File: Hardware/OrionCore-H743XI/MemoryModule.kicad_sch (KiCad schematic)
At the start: 3 parts, among them U1 IS42S32800G-6BLI, U3 W25Q128JVP, U4 W25Q128JVP

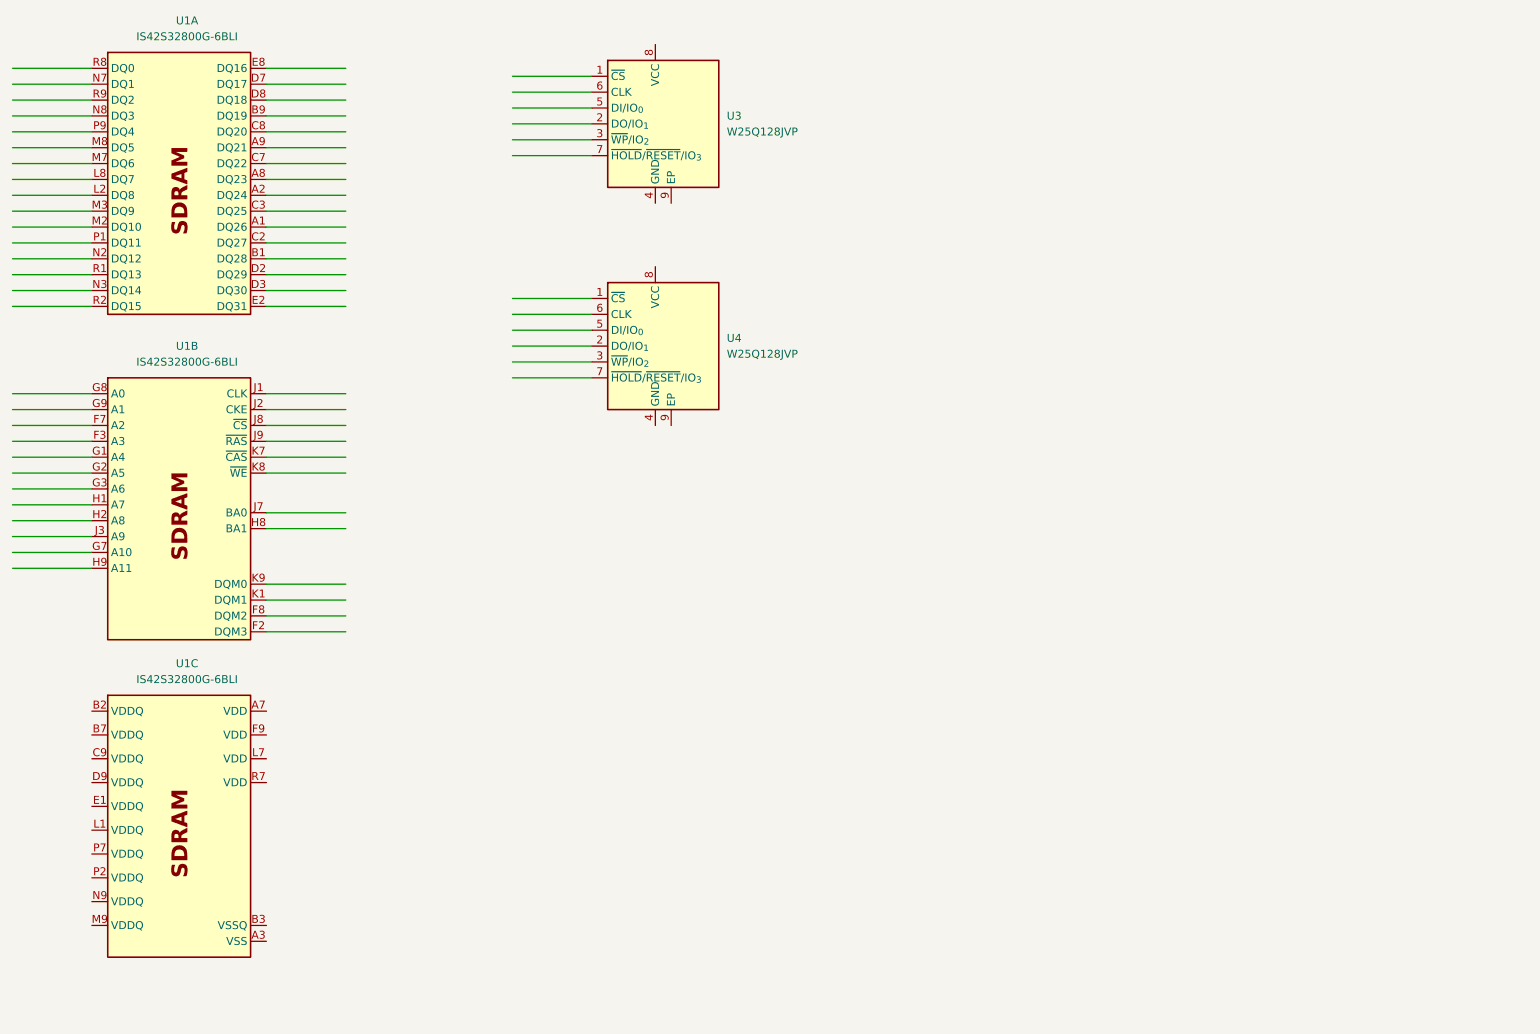
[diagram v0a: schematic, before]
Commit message: Update SDRAM, RGB LCD, QSPI Flash Pin
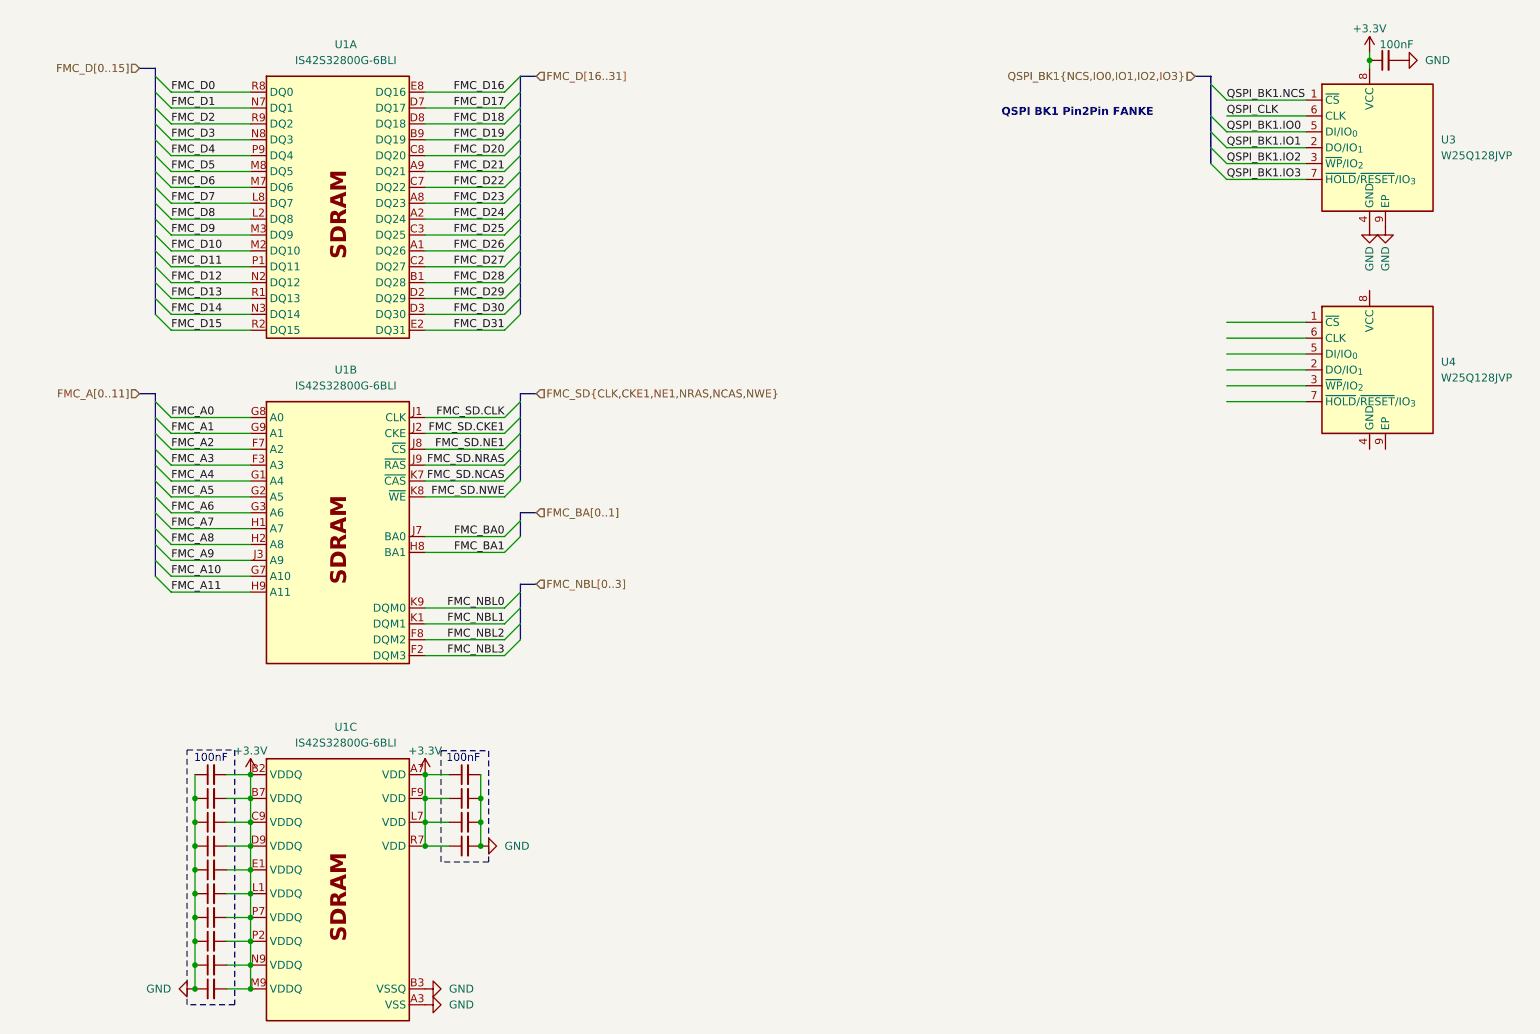
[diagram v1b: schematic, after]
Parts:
- added C30, C31, C32, C33, C34, C35, C36, C37, C38, C39, C40, C41, C42, C43, C44: 100nF, Capacitor_SMD:C_0201_0603Metric, symbol Device:C_Small
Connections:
- net VSS is gone; now on net GND: U1.A3 (VSS), U1.F1 (VSS), U1.L3 (VSS), U1.R3 (VSS)
- net VSSQ is gone; now on net GND: U1.B3 (VSSQ), U1.B8 (VSSQ), U1.C1 (VSSQ), U1.D1 (VSSQ), U1.E9 (VSSQ), U1.L9 (VSSQ), U1.M1 (VSSQ), U1.N1 (VSSQ), U1.P3 (VSSQ), U1.P8 (VSSQ)
- net QSPI_BK1.NCS: now reaches U3.1 (~{CS})
- net QSPI_BK1.IO1: now reaches U3.2 (DO/IO_{1})
- net QSPI_BK1.IO2: now reaches U3.3 (~{WP}/IO_{2})
- net GND: now reaches U3.4 (GND)
- net GND: now also U3.9 (EP), C30.1, C31.1, C32.1, C33.1, C34.1, C35.1, C36.1, C37.1, C38.1, C39.1, C40.2, C41.2, C42.2, C43.2, C44.2
- net QSPI_BK1.IO0: now reaches U3.5 (DI/IO_{0})
- net QSPI_CLK: now reaches U3.6 (CLK)
- net QSPI_BK1.IO3: now reaches U3.7 (~{HOLD}/~{RESET}/IO_{3})
- net +3.3V: now reaches U3.8 (VCC)
- net +3.3V: now also U1.A7 (VDD), U1.B2 (VDDQ), U1.B7 (VDDQ), U1.C9 (VDDQ), U1.D9 (VDDQ), U1.E1 (VDDQ), U1.F9 (VDD), U1.L1 (VDDQ), U1.L7 (VDD), U1.M9 (VDDQ), U1.N9 (VDDQ), U1.P2 (VDDQ), U1.P7 (VDDQ), U1.R7 (VDD), C30.2, C31.2, C32.2, C33.2, C34.2, C35.2, C36.2, C37.2, C38.2, C39.2, C40.1, C41.1, C42.1, C43.1, C44.1
- net FMC_D26: now reaches U1.A1 (DQ26)
- net FMC_D24: now reaches U1.A2 (DQ24)
- net FMC_D23: now reaches U1.A8 (DQ23)
- net FMC_D21: now reaches U1.A9 (DQ21)
- net FMC_D28: now reaches U1.B1 (DQ28)
- net FMC_D19: now reaches U1.B9 (DQ19)
- net FMC_D27: now reaches U1.C2 (DQ27)
- net FMC_D25: now reaches U1.C3 (DQ25)
- net FMC_D22: now reaches U1.C7 (DQ22)
- net FMC_D20: now reaches U1.C8 (DQ20)
- net FMC_D29: now reaches U1.D2 (DQ29)
- net FMC_D30: now reaches U1.D3 (DQ30)
- net FMC_D17: now reaches U1.D7 (DQ17)
- net FMC_D18: now reaches U1.D8 (DQ18)
- net FMC_D31: now reaches U1.E2 (DQ31)
- net FMC_D16: now reaches U1.E8 (DQ16)
- net FMC_D8: now reaches U1.L2 (DQ8)
- net FMC_D7: now reaches U1.L8 (DQ7)
- net FMC_D10: now reaches U1.M2 (DQ10)
- net FMC_D9: now reaches U1.M3 (DQ9)
- net FMC_D6: now reaches U1.M7 (DQ6)
- net FMC_D5: now reaches U1.M8 (DQ5)
- net FMC_D12: now reaches U1.N2 (DQ12)
- net FMC_D14: now reaches U1.N3 (DQ14)
- net FMC_D1: now reaches U1.N7 (DQ1)
- net FMC_D3: now reaches U1.N8 (DQ3)
- net FMC_D11: now reaches U1.P1 (DQ11)
- net FMC_D4: now reaches U1.P9 (DQ4)
- net FMC_D13: now reaches U1.R1 (DQ13)
- net FMC_D15: now reaches U1.R2 (DQ15)
- net FMC_D0: now reaches U1.R8 (DQ0)
- net FMC_D2: now reaches U1.R9 (DQ2)
- net FMC_NBL3: now reaches U1.F2 (DQM3)
- net FMC_A3: now reaches U1.F3 (A3)
- net FMC_A2: now reaches U1.F7 (A2)
- net FMC_NBL2: now reaches U1.F8 (DQM2)
- net FMC_A4: now reaches U1.G1 (A4)
- net FMC_A5: now reaches U1.G2 (A5)
- net FMC_A6: now reaches U1.G3 (A6)
- net FMC_A10: now reaches U1.G7 (A10)
- net FMC_A0: now reaches U1.G8 (A0)
- net FMC_A1: now reaches U1.G9 (A1)
- net FMC_A7: now reaches U1.H1 (A7)
- net FMC_A8: now reaches U1.H2 (A8)
- net FMC_BA1: now reaches U1.H8 (BA1)
- net FMC_A11: now reaches U1.H9 (A11)
- net FMC_SD.CLK: now reaches U1.J1 (CLK)
- net FMC_SD.CKE1: now reaches U1.J2 (CKE)
- net FMC_A9: now reaches U1.J3 (A9)
- net FMC_BA0: now reaches U1.J7 (BA0)
- net FMC_SD.NE1: now reaches U1.J8 (~{CS})
- net FMC_SD.NRAS: now reaches U1.J9 (~{RAS})
- net FMC_NBL1: now reaches U1.K1 (DQM1)
- net FMC_SD.NCAS: now reaches U1.K7 (~{CAS})
- net FMC_SD.NWE: now reaches U1.K8 (~{WE})
- net FMC_NBL0: now reaches U1.K9 (DQM0)
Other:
- note added: "100nF"
- note added: "QSPI BK1 Pin2Pin FANKE"
- moved on the sheet: U1A, U1B, U1C, U3, U4

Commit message: feat: update dual qspi
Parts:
- added C45: 100nF, Capacitor_SMD:C_0201_0603Metric, symbol Device:C_Small
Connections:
- net +3.3V: now also U4.8 (VCC), C45.1
- net GND: now also U4.4 (GND), U4.9 (EP), C45.2
- net QSPI_CLK: now also U4.6 (CLK)
- net QSPI_BK2.NCS: now reaches U4.1 (~{CS})
- net QSPI_BK2.IO1: now reaches U4.2 (DO/IO_{1})
- net QSPI_BK2.IO2: now reaches U4.3 (~{WP}/IO_{2})
- net QSPI_BK2.IO0: now reaches U4.5 (DI/IO_{0})
- net QSPI_BK2.IO3: now reaches U4.7 (~{HOLD}/~{RESET}/IO_{3})
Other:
- company: (none) -> Peakors
- title: (none) -> OrionCore
- moved on the sheet: U4
